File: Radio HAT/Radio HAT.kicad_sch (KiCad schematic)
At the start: 40 parts, among them J1 Raspberry_Pi_2_3, J2 Coax SMA, J3 Barrel_Jack, J4 VCC, J5 6V, J6 GND, J7 V_RF, J8 GPIO, Q1 NMOS, U1 RFM98PW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

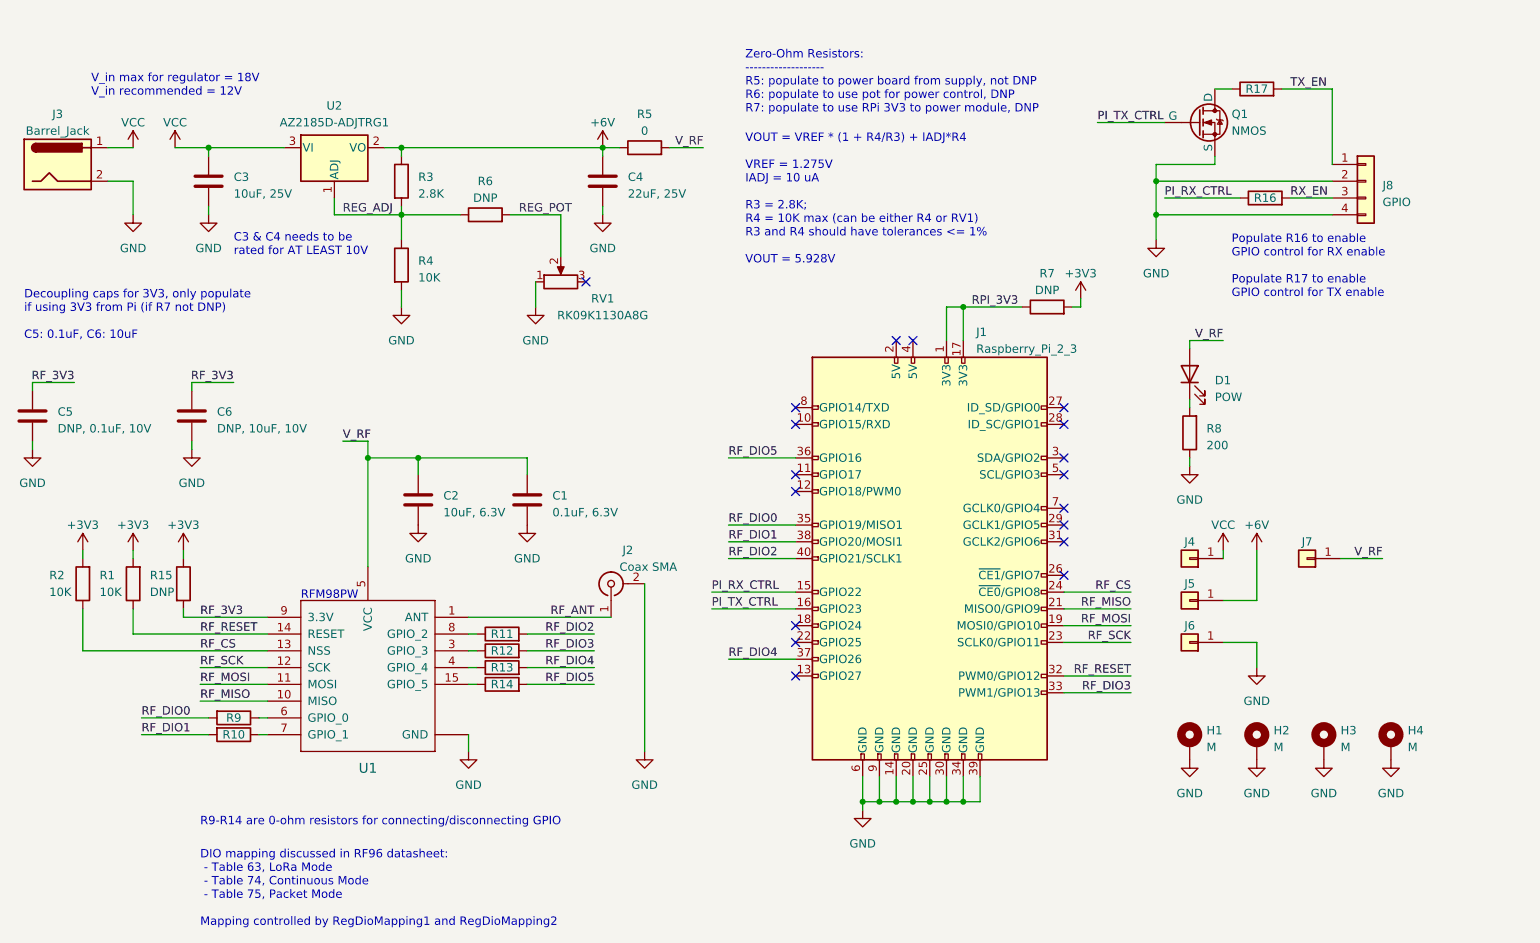
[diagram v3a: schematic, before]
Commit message: Added stitching vias
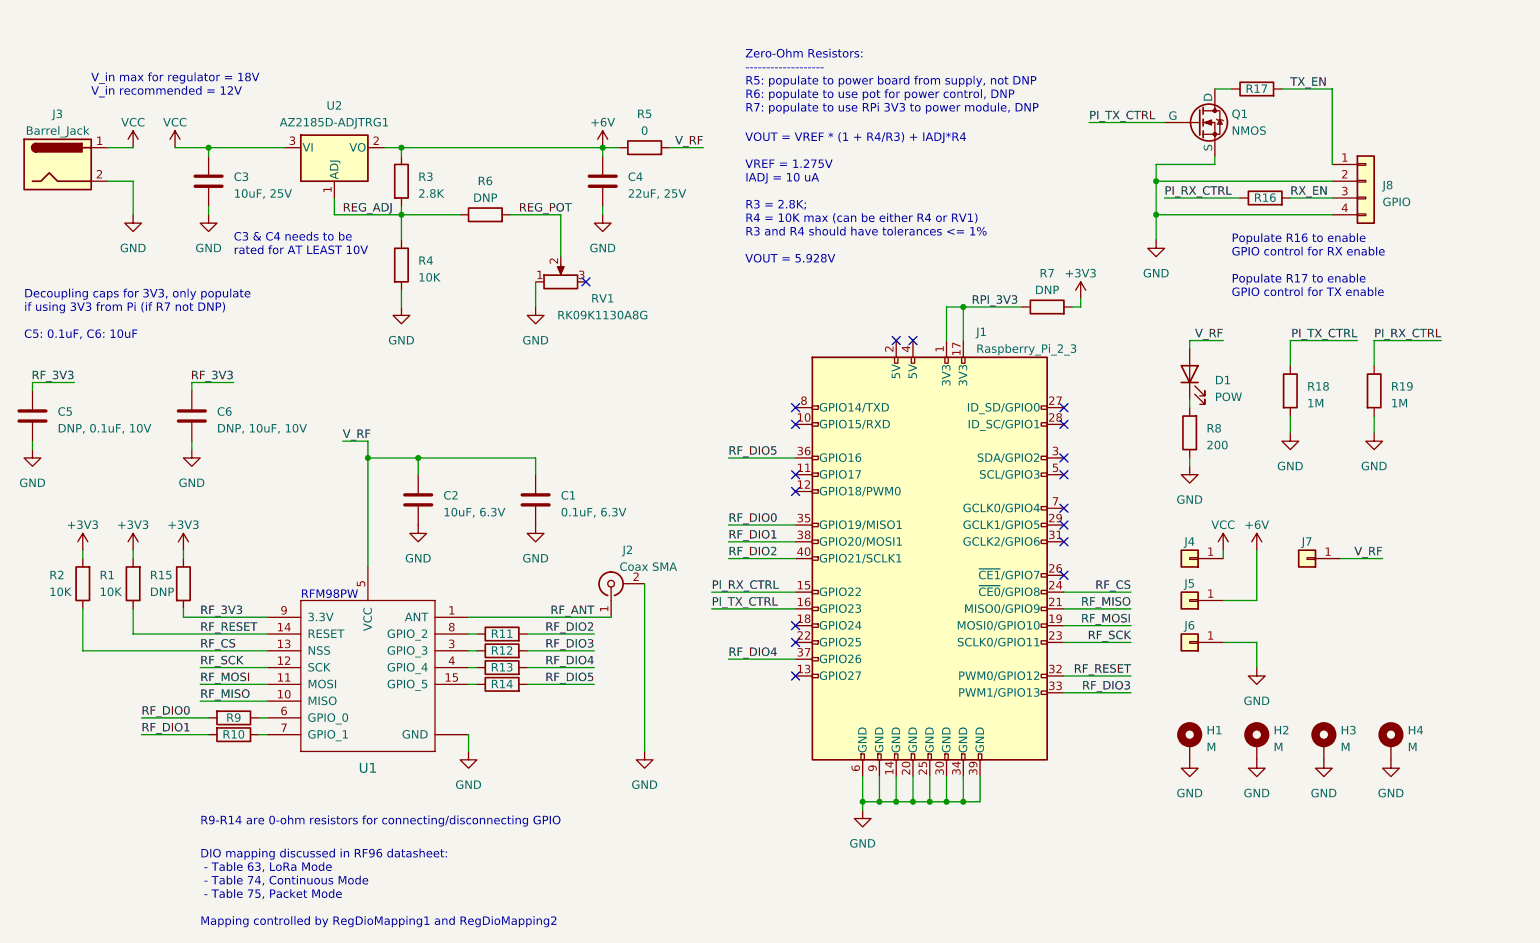
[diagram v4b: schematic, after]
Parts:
- added R18, R19: 1M, Resistor_SMD:R_0805_2012Metric_Pad1.20x1.40mm_HandSolder, symbol Device:R
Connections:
- net GND: now also R18.2, R19.2
- net PI_RX_CTRL: now also R19.1
- net PI_TX_CTRL: now also R18.1
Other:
- moved on the sheet: C1
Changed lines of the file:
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@@
     (stroke (width 0) (type default))
   )
-  (wire (pts (xy 106.68 90.17) (xy 123.19 90.17))
+  (wire (pts (xy 106.68 90.17) (xy 124.46 90.17))
     (stroke (width 0) (type default))
   )
@@
     (stroke (width 0) (type default))
   )
+  (wire (pts (xy 238.76 83.82) (xy 238.76 86.36))
+    (stroke (width 0) (type default))
+  )
   (wire (pts (xy 72.39 87.63) (xy 72.39 88.9))
     (stroke (width 0) (type default))
@@
     (stroke (width 0) (type default))
   )
+  (wire (pts (xy 251.46 76.2) (xy 251.46 72.39))
+    (stroke (width 0) (type default))
+  )
   (wire (pts (xy 134.62 43.18) (xy 137.16 43.18))
     (stroke (width 0) (type default))
@@
     (stroke (width 0) (type default))
   )
+  (wire (pts (xy 251.46 72.39) (xy 261.62 72.39))
+    (stroke (width 0) (type default))
+  )
   (wire (pts (xy 114.3 132.08) (xy 114.3 134.62))
     (stroke (width 0) (type default))
   )
+  (wire (pts (xy 238.76 76.2) (xy 238.76 72.39))
+    (stroke (width 0) (type default))
+  )
   (wire (pts (xy 99.06 90.17) (xy 106.68 90.17))
     (stroke (width 0) (type default))
@@
     (stroke (width 0) (type default))
   )
+  (wire (pts (xy 251.46 83.82) (xy 251.46 86.36))
+    (stroke (width 0) (type default))
+  )
   (wire (pts (xy 218.44 53.34) (xy 245.11 53.34))
     (stroke (width 0) (type default))
@@
     (stroke (width 0) (type default))
   )
-  (wire (pts (xy 123.19 90.17) (xy 123.19 92.71))
+  (wire (pts (xy 124.46 90.17) (xy 124.46 92.71))
     (stroke (width 0) (type default))
   )
@@
     (stroke (width 0) (type default))
   )
-  (wire (pts (xy 209.55 39.37) (xy 219.71 39.37))
+  (wire (pts (xy 208.28 39.37) (xy 219.71 39.37))
     (stroke (width 0) (type default))
   )
@@
   )
   (wire (pts (xy 134.62 43.18) (xy 134.62 44.45))
+    (stroke (width 0) (type default))
+  )
+  (wire (pts (xy 238.76 72.39) (xy 248.92 72.39))
     (stroke (width 0) (type default))
   )
@@
     (effects (font (size 1.27 1.27)) (justify left bottom))
   )
-  (label "PI_TX_CTRL" (at 209.55 39.37 0) (fields_autoplaced)
+  (label "PI_TX_CTRL" (at 208.28 39.37 0) (fields_autoplaced)
     (effects (font (size 1.27 1.27)) (justify left bottom))
   )
@@
     (effects (font (size 1.27 1.27)) (justify right bottom))
   )
+  (label "PI_RX_CTRL" (at 261.62 72.39 180) (fields_autoplaced)
+    (effects (font (size 1.27 1.27)) (justify right bottom))
+  )
   (label "REG_ADJ" (at 95.25 53.34 0) (fields_autoplaced)
     (effects (font (size 1.27 1.27)) (justify left bottom))
@@
     (effects (font (size 1.27 1.27)) (justify right bottom))
   )
+  (label "PI_TX_CTRL" (at 248.92 72.39 180) (fields_autoplaced)
+    (effects (font (size 1.27 1.27)) (justify right bottom))
+  )
   (label "RF_CS" (at 73.66 119.38 0) (fields_autoplaced)
     (effects (font (size 1.27 1.27)) (justify left bottom))
@@
     )
   )
+  (symbol (lib_id "power:GND") (at 238.76 86.36 0) (unit 1)
+    (in_bom yes) (on_board yes) (dnp no)
+    (property "Reference" "#PWR025" (at 238.76 92.71 0)
+      (effects (font (size 1.27 1.27)) hide)
+    )
+    (property "Value" "GND" (at 238.76 91.44 0)
+      (effects (font (size 1.27 1.27)))
+    )
+    (property "Footprint" "" (at 238.76 86.36 0)
+      (effects (font (size 1.27 1.27)) hide)
+    )
+    (property "Datasheet" "" (at 238.76 86.36 0)
+      (effects (font (size 1.27 1.27)) hide)
+    )
+    (pin "1")
+    (instances
+      (project "Radio HAT"
+        (path "/e833ba5c-90ae-4111-9eec-1a872963763a"
+          (reference "#PWR025") (unit 1)
+        )
+      )
+    )
+  )
   (symbol (lib_id "power:+3V3") (at 55.88 104.14 0) (unit 1)
     (in_bom yes) (on_board yes) (dnp no) (fields_autoplaced)
@@
     )
   )
+  (symbol (lib_id "power:GND") (at 251.46 86.36 0) (unit 1)
+    (in_bom yes) (on_board yes) (dnp no)
+    (property "Reference" "#PWR030" (at 251.46 92.71 0)
+      (effects (font (size 1.27 1.27)) hide)
+    )
+    (property "Value" "GND" (at 251.46 91.44 0)
+      (effects (font (size 1.27 1.27)))
+    )
+    (property "Footprint" "" (at 251.46 86.36 0)
+      (effects (font (size 1.27 1.27)) hide)
+    )
+    (property "Datasheet" "" (at 251.46 86.36 0)
+      (effects (font (size 1.27 1.27)) hide)
+    )
+    (pin "1")
+    (instances
+      (project "Radio HAT"
+        (path "/e833ba5c-90ae-4111-9eec-1a872963763a"
+          (reference "#PWR030") (unit 1)
+        )
+      )
+    )
+  )
   (symbol (lib_id "Device:R") (at 78.74 132.08 270) (unit 1)
     (in_bom yes) (on_board yes) (dnp no)
@@
         (path "/e833ba5c-90ae-4111-9eec-1a872963763a"
           (reference "R10") (unit 1)
+        )
+      )
+    )
+  )
+  (symbol (lib_id "Device:R") (at 251.46 80.01 0) (unit 1)
+    (in_bom yes) (on_board yes) (dnp no) (fields_autoplaced)
+    (property "Reference" "R19" (at 254 79.375 0)
+      (effects (font (size 1.27 1.27)) (justify left))
+    )
+    (property "Value" "1M" (at 254 81.915 0)
+      (effects (font (size 1.27 1.27)) (justify left))
+    )
+    (property "Footprint" "Resistor_SMD:R_0805_2012Metric_Pad1.20x1.40mm_HandSolder" (at 249.682 80.01 90)
+      (effects (font (size 1.27 1.27)) hide)
+    )
+    (property "Datasheet" "~" (at 251.46 80.01 0)
+      (effects (font (size 1.27 1.27)) hide)
+    )
+    (pin "1")
+    (pin "2")
+    (instances
+      (project "Radio HAT"
+        (path "/e833ba5c-90ae-4111-9eec-1a872963763a"
+          (reference "R19") (unit 1)
         )
       )
@@
     )
   )
-  (symbol (lib_id "power:GND") (at 123.19 100.33 0) (unit 1)
-    (in_bom yes) (on_board yes) (dnp no)
-    (property "Reference" "#PWR010" (at 123.19 106.68 0)
-      (effects (font (size 1.27 1.27)) hide)
-    )
-    (property "Value" "GND" (at 123.19 105.41 0)
-      (effects (font (size 1.27 1.27)))
-    )
-    (property "Footprint" "" (at 123.19 100.33 0)
-      (effects (font (size 1.27 1.27)) hide)
-    )
-    (property "Datasheet" "" (at 123.19 100.33 0)
+  (symbol (lib_id "power:GND") (at 124.46 100.33 0) (unit 1)
+    (in_bom yes) (on_board yes) (dnp no)
+    (property "Reference" "#PWR010" (at 124.46 106.68 0)
+      (effects (font (size 1.27 1.27)) hide)
+    )
+    (property "Value" "GND" (at 124.46 105.41 0)
+      (effects (font (size 1.27 1.27)))
+    )
+    (property "Footprint" "" (at 124.46 100.33 0)
+      (effects (font (size 1.27 1.27)) hide)
+    )
+    (property "Datasheet" "" (at 124.46 100.33 0)
       (effects (font (size 1.27 1.27)) hide)
     )
@@
     )
   )
+  (symbol (lib_id "Device:R") (at 238.76 80.01 0) (unit 1)
+    (in_bom yes) (on_board yes) (dnp no) (fields_autoplaced)
+    (property "Reference" "R18" (at 241.3 79.375 0)
+      (effects (font (size 1.27 1.27)) (justify left))
+    )
+    (property "Value" "1M" (at 241.3 81.915 0)
+      (effects (font (size 1.27 1.27)) (justify left))
+    )
+    (property "Footprint" "Resistor_SMD:R_0805_2012Metric_Pad1.20x1.40mm_HandSolder" (at 236.982 80.01 90)
+      (effects (font (size 1.27 1.27)) hide)
+    )
+    (property "Datasheet" "~" (at 238.76 80.01 0)
+      (effects (font (size 1.27 1.27)) hide)
+    )
+    (pin "1")
+    (pin "2")
+    (instances
+      (project "Radio HAT"
+        (path "/e833ba5c-90ae-4111-9eec-1a872963763a"
+          (reference "R18") (unit 1)
+        )
+      )
+    )
+  )
   (symbol (lib_id "power:+3V3") (at 207.01 66.04 0) (unit 1)
     (in_bom yes) (on_board yes) (dnp no) (fields_autoplaced)
@@
     )
   )
-  (symbol (lib_id "Device:C") (at 123.19 96.52 0) (unit 1)
-    (in_bom yes) (on_board yes) (dnp no) (fields_autoplaced)
-    (property "Reference" "C1" (at 127 95.885 0)
-      (effects (font (size 1.27 1.27)) (justify left))
-    )
-    (property "Value" "0.1uF, 6.3V" (at 127 98.425 0)
-      (effects (font (size 1.27 1.27)) (justify left))
-    )
-    (property "Footprint" "Capacitor_SMD:C_0603_1608Metric_Pad1.08x0.95mm_HandSolder" (at 124.1552 100.33 0)
-      (effects (font (size 1.27 1.27)) hide)
-    )
-    (property "Datasheet" "~" (at 123.19 96.52 0)
-      (effects (font (size 1.27 1.27)) hide)
-    )
+  (symbol (lib_id "Device:C") (at 124.46 96.52 0) (unit 1)
+    (in_bom yes) (on_board yes) (dnp no) (fields_autoplaced)
+    (property "Reference" "C1" (at 128.27 95.885 0)
+      (effects (font (size 1.27 1.27)) (justify left))
+    )
+    (property "Value" "0.1uF, 6.3V" (at 128.27 98.425 0)
+      (effects (font (size 1.27 1.27)) (justify left))
+    )
+    (property "Footprint" "Capacitor_SMD:C_0603_1608Metric_Pad1.08x0.95mm_HandSolder" (at 125.4252 100.33 0)
+      (effects (font (size 1.27 1.27)) hide)
+    )
+    (property "Datasheet" "~" (at 124.46 96.52 0)
+      (effects (font (size 1.27 1.27)) hide)
+    )

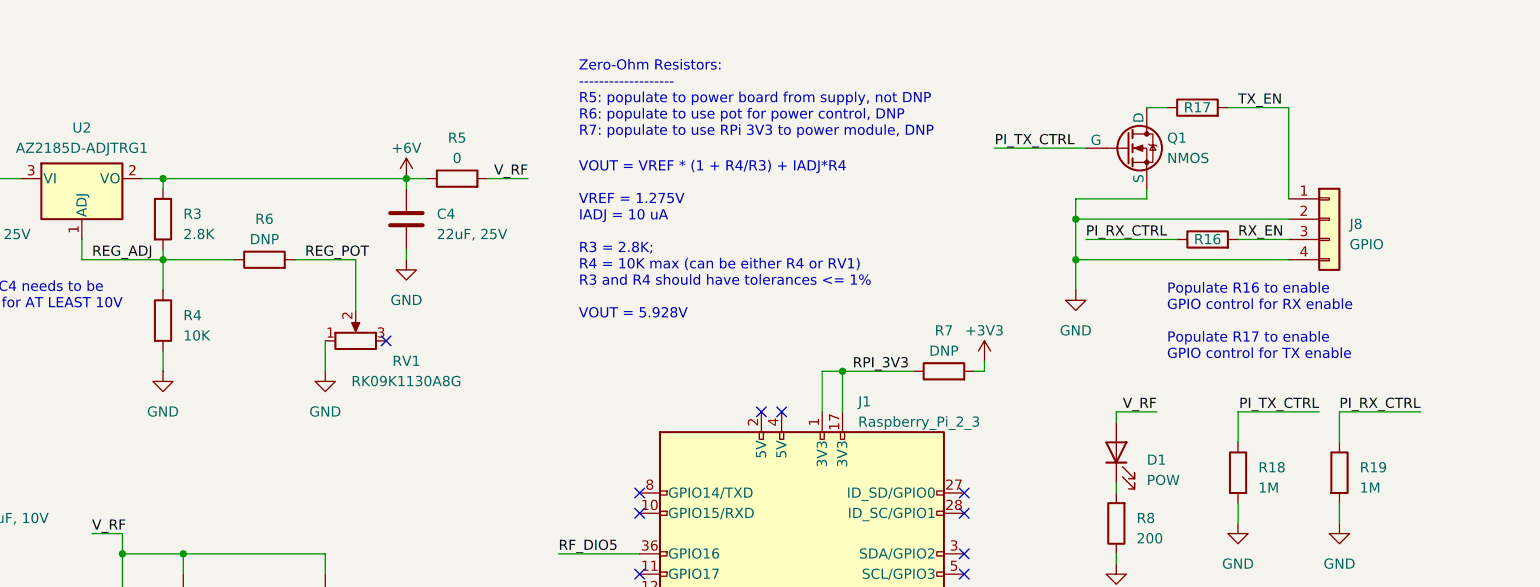
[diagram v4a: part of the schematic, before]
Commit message: Add bypass resistor on TX GPIO control, ground Pot
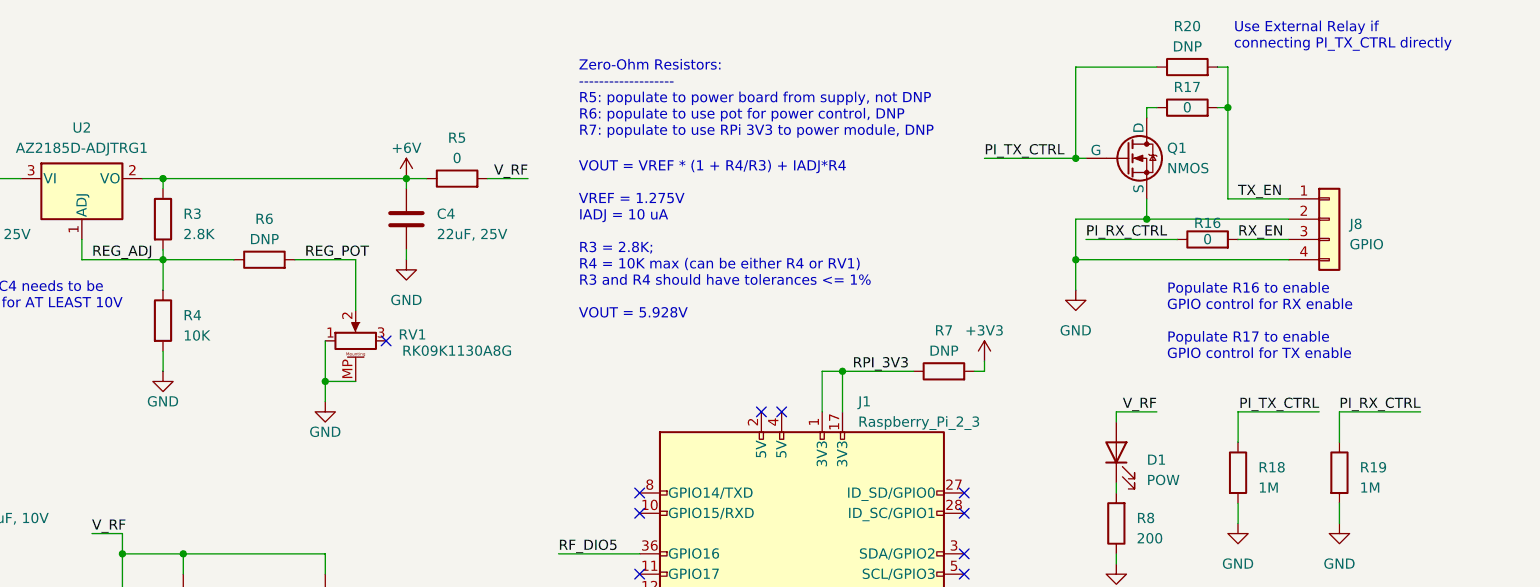
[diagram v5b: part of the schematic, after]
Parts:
- added R20: DNP, Resistor_SMD:R_0805_2012Metric_Pad1.20x1.40mm_HandSolder, symbol Device:R
- R16, R17: value DNP -> 0
- RV1: symbol Device:R_Potentiometer -> Device:R_Potentiometer_MountingPin
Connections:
- net GND: now also RV1.MP (MountPin)
- net PI_TX_CTRL: now also R20.1
- net TX_EN: now also R20.2
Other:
- note added: "Use External Relay if connecting PI_TX_CTRL directly"
- moved on the sheet: Q1, R17
